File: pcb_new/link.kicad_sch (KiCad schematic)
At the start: 90 parts, among them J1 STLINK-V3MINIE, J11 68021-204HLF, J12 68021-204HLF, J13 68021-204HLF, J15 68021-204HLF, J16 68021-204HLF, J17 68021-204HLF, J18 68021-204HLF, SW1 TL6400AF160QJ, U1 STM32F479VGT6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

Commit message: initial test of new board
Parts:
- C32, C33, C34: Mouser Part Number 81-GRM15C61E475ME15J -> (none)
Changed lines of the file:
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@@
 			)
 		)
-		(property "Mouser Part Number" "81-GRM15C61E475ME15J"
+		(property "Mouser Part Number" ""
 			(at 388.62 806.68 0)
 			(effects
@@
 			)
 		)
-		(property "Mouser Part Number" "81-GRM15C61E475ME15J"
+		(property "Mouser Part Number" ""
 			(at 388.62 796.52 0)
 			(effects
@@
 			)
 		)
-		(property "Mouser Part Number" "81-GRM15C61E475ME15J"
+		(property "Mouser Part Number" ""
 			(at 388.62 801.6 0)
 			(effects

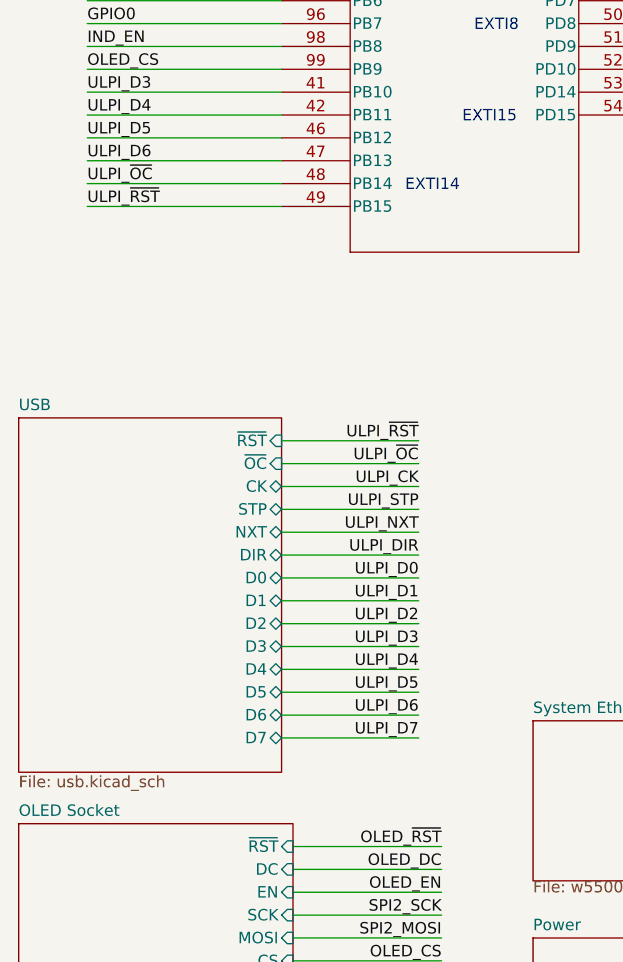
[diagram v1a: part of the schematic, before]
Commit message: don't mark `ULPI_~{OC}` as a ULPI netclass
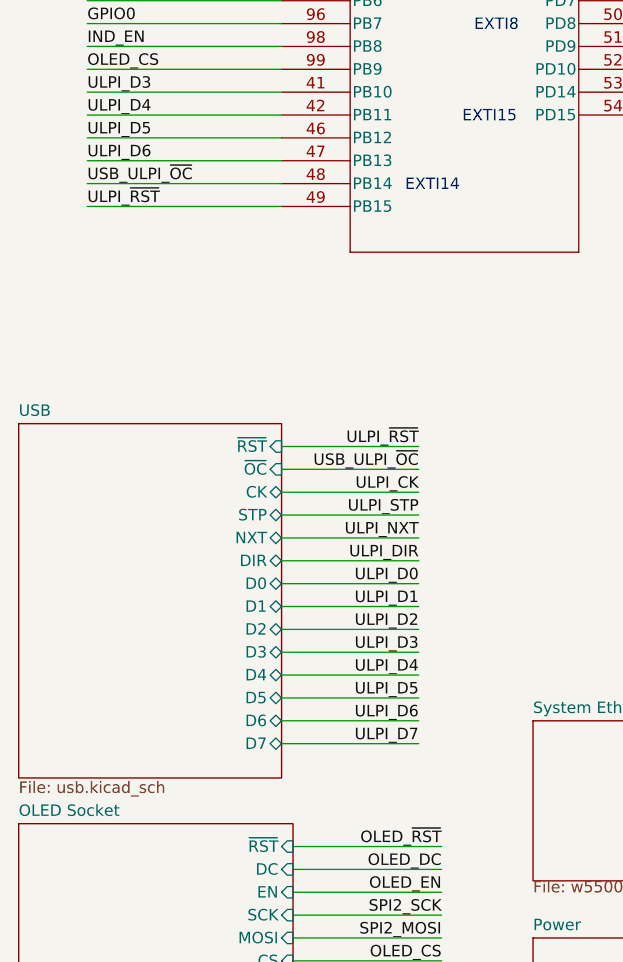
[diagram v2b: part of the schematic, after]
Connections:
- net ULPI_~{OC} renamed USB_ULPI_~{OC}
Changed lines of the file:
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@@
 	(wire
 		(pts
-			(xy 54.61 168.275) (xy 69.85 168.275)
+			(xy 54.61 168.91) (xy 69.85 168.91)
 		)
 		(stroke
@@
 	(wire
 		(pts
-			(xy 54.61 173.355) (xy 69.85 173.355)
+			(xy 54.61 173.99) (xy 69.85 173.99)
 		)
 		(stroke
@@
 	(wire
 		(pts
-			(xy 54.61 155.575) (xy 69.85 155.575)
+			(xy 54.61 156.21) (xy 69.85 156.21)
 		)
 		(stroke
@@
 	(wire
 		(pts
-			(xy 54.61 180.975) (xy 69.85 180.975)
+			(xy 54.61 181.61) (xy 69.85 181.61)
 		)
 		(stroke
@@
 	(wire
 		(pts
-			(xy 54.61 165.735) (xy 69.85 165.735)
+			(xy 54.61 166.37) (xy 69.85 166.37)
 		)
 		(stroke
@@
 	(wire
 		(pts
-			(xy 54.61 160.655) (xy 69.85 160.655)
+			(xy 54.61 161.29) (xy 69.85 161.29)
 		)
 		(stroke
@@
 	(wire
 		(pts
-			(xy 54.61 178.435) (xy 69.85 178.435)
+			(xy 54.61 179.07) (xy 69.85 179.07)
 		)
 		(stroke
@@
 	(wire
 		(pts
-			(xy 54.61 186.055) (xy 69.85 186.055)
+			(xy 54.61 186.69) (xy 69.85 186.69)
 		)
 		(stroke
@@
 	(wire
 		(pts
-			(xy 54.61 175.895) (xy 69.85 175.895)
+			(xy 54.61 176.53) (xy 69.85 176.53)
 		)
 		(stroke
@@
 	(wire
 		(pts
-			(xy 54.61 170.815) (xy 69.85 170.815)
+			(xy 54.61 171.45) (xy 69.85 171.45)
 		)
 		(stroke
@@
 	(wire
 		(pts
-			(xy 54.61 183.515) (xy 69.85 183.515)
+			(xy 54.61 184.15) (xy 69.85 184.15)
 		)
 		(stroke
@@
 	(wire
 		(pts
-			(xy 54.61 158.115) (xy 69.85 158.115)
+			(xy 54.61 158.75) (xy 69.85 158.75)
 		)
 		(stroke
@@
 	(wire
 		(pts
-			(xy 54.61 188.595) (xy 69.85 188.595)
+			(xy 54.61 189.23) (xy 69.85 189.23)
 		)
 		(stroke
@@
 	(wire
 		(pts
-			(xy 54.61 163.195) (xy 69.85 163.195)
+			(xy 54.61 163.83) (xy 69.85 163.83)
 		)
 		(stroke
@@
 	)
 	(label "ULPI_D2"
-		(at 69.85 175.895 180)
+		(at 69.85 176.53 180)
 		(fields_autoplaced yes)
 		(effects
@@
 	)
 	(label "ULPI_D1"
-		(at 69.85 173.355 180)
+		(at 69.85 173.99 180)
 		(fields_autoplaced yes)
 		(effects
@@
 		)
 	)
-	(label "OLED_CS"
-		(at 162.56 146.05 0)
+	(label "USB_ULPI_~{OC}"
+		(at 69.85 158.75 180)
 		(fields_autoplaced yes)
 		(effects
@@
 				(size 1.27 1.27)
 			)
-			(justify left bottom)
+			(justify right bottom)
 		)
 	)
-	(label "RS232_TX"
-		(at 187.96 273.05 0)
+	(label "OLED_CS"
+		(at 162.56 146.05 0)
 		(fields_autoplaced yes)
 		(effects
@@
 		)
 	)
-	(label "SPI3_MISO"
-		(at 74.93 233.68 180)
+	(label "RS232_TX"
+		(at 187.96 273.05 0)
 		(fields_autoplaced yes)
 		(effects
@@
 				(size 1.27 1.27)
 			)
-			(justify right bottom)
+			(justify left bottom)
 		)
 	)
-	(label "ULPI_~{OC}"
-		(at 69.85 158.115 180)
+	(label "SPI3_MISO"
+		(at 74.93 233.68 180)
 		(fields_autoplaced yes)
 		(effects
@@
 	)
 	(label "ULPI_D5"
-		(at 69.85 183.515 180)
+		(at 69.85 184.15 180)
 		(fields_autoplaced yes)
 		(effects
@@
 	)
 	(label "ULPI_CK"
-		(at 69.85 160.655 180)
+		(at 69.85 161.29 180)
 		(fields_autoplaced yes)
 		(effects
@@
 	)
 	(label "ULPI_NXT"
-		(at 69.85 165.735 180)
+		(at 69.85 166.37 180)
 		(fields_autoplaced yes)
 		(effects
@@
 		)
 	)
-	(label "ULPI_~{OC}"
+	(label "USB_ULPI_~{OC}"
 		(at 33.02 127 0)
 		(fields_autoplaced yes)
@@
 	)
 	(label "ULPI_D3"
-		(at 69.85 178.435 180)
+		(at 69.85 179.07 180)
 		(fields_autoplaced yes)
 		(effects
@@
 	)
 	(label "ULPI_D6"
-		(at 69.85 186.055 180)
+		(at 69.85 186.69 180)
 		(fields_autoplaced yes)
 		(effects
@@
 	)
 	(label "ULPI_DIR"
-		(at 69.85 168.275 180)
+		(at 69.85 168.91 180)
 		(fields_autoplaced yes)
 		(effects
@@
 	)
 	(label "ULPI_STP"
-		(at 69.85 163.195 180)
+		(at 69.85 163.83 180)
 		(fields_autoplaced yes)
 		(effects
@@
 	)
 	(label "ULPI_D0"
-		(at 69.85 170.815 180)
+		(at 69.85 171.45 180)
 		(fields_autoplaced yes)
 		(effects
@@
 	)
 	(label "ULPI_D4"
-		(at 69.85 180.975 180)
+		(at 69.85 181.61 180)
 		(fields_autoplaced yes)
 		(effects
@@
 	)
 	(label "ULPI_~{RST}"
-		(at 69.85 155.575 180)
+		(at 69.85 156.21 180)
 		(fields_autoplaced yes)
 		(effects
@@
 	)
 	(label "ULPI_D7"
-		(at 69.85 188.595 180)
+		(at 69.85 189.23 180)
 		(fields_autoplaced yes)
 		(effects
@@
 	)
 	(sheet
-		(at 25.4 153.035)
+		(at 25.4 153.67)
 		(size 29.21 39.37)
 		(fields_autoplaced yes)
@@
 		)
 		(property "Sheetname" "USB"
-			(at 25.4 152.3234 0)
+			(at 25.4 152.9584 0)
 			(effects
 				(font
@@
 		)
 		(property "Sheetfile" "usb.kicad_sch"
-			(at 25.4 192.7356 0)
+			(at 25.4 193.3706 0)
 			(effects
 				(font
@@
 		)
 		(pin "CK" bidirectional
-			(at 54.61 160.655 0)
+			(at 54.61 161.29 0)
 			(effects
 				(font
@@
 		)
 		(pin "STP" bidirectional
-			(at 54.61 163.195 0)
+			(at 54.61 163.83 0)
 			(effects
 				(font
@@
 		)
 		(pin "NXT" bidirectional
-			(at 54.61 165.735 0)
+			(at 54.61 166.37 0)
 			(effects
 				(font
@@
 		)
 		(pin "DIR" bidirectional
-			(at 54.61 168.275 0)
+			(at 54.61 168.91 0)
 			(effects
 				(font
@@
 		)
 		(pin "D5" bidirectional
-			(at 54.61 183.515 0)
+			(at 54.61 184.15 0)
 			(effects
 				(font
@@
 		)
 		(pin "D4" bidirectional
-			(at 54.61 180.975 0)
+			(at 54.61 181.61 0)
 			(effects
 				(font
@@
 		)
 		(pin "D6" bidirectional
-			(at 54.61 186.055 0)
+			(at 54.61 186.69 0)
 			(effects
 				(font
@@
 		)
 		(pin "D0" bidirectional
-			(at 54.61 170.815 0)
+			(at 54.61 171.45 0)
 			(effects
 				(font
@@
 		)
 		(pin "D3" bidirectional
-			(at 54.61 178.435 0)
+			(at 54.61 179.07 0)
 			(effects
 				(font
@@
 		)
 		(pin "D2" bidirectional
-			(at 54.61 175.895 0)
+			(at 54.61 176.53 0)
 			(effects
 				(font
@@
 		)
 		(pin "D1" bidirectional
-			(at 54.61 173.355 0)
+			(at 54.61 173.99 0)
 			(effects
 				(font
@@
 		)
 		(pin "~{OC}" input
-			(at 54.61 158.115 0)
+			(at 54.61 158.75 0)
 			(effects
 				(font
@@
 		)
 		(pin "D7" bidirectional
-			(at 54.61 188.595 0)
+			(at 54.61 189.23 0)
 			(effects
 				(font
@@
 		)
 		(pin "~{RST}" input
-			(at 54.61 155.575 0)
+			(at 54.61 156.21 0)
 			(effects
 				(font

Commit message: add power monitor alert interrupt line (ref #82)
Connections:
- net GPIO4: no longer names the net of J15.1
- net GPIO4: no longer U1.34 (PE9)
- new net ~{POWER_ALERT}: U1.34 (PE9)
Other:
- sheet Power ports: added ~{ALERT}; removed none
- note added: "EXTI9"
- note added: "TBD"
- moved on the sheet: R1, R2

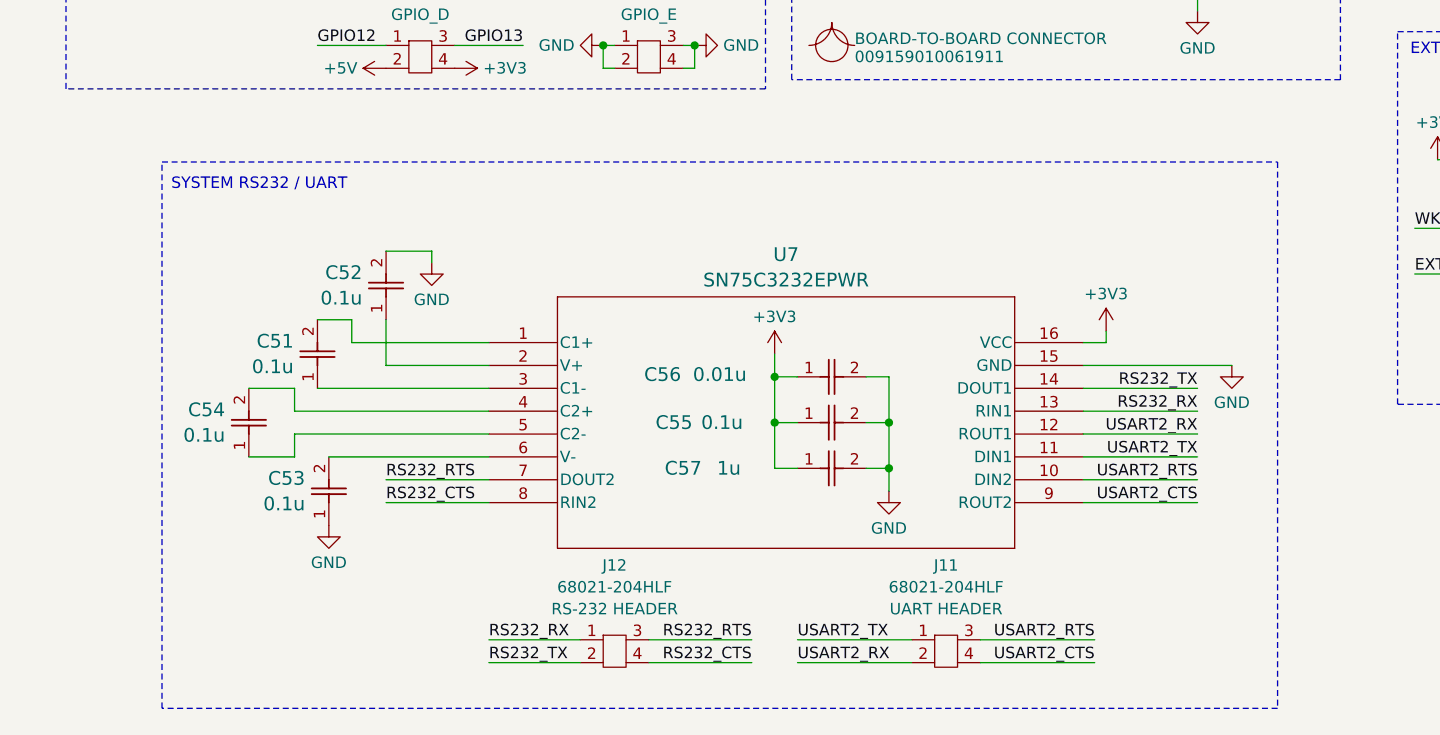
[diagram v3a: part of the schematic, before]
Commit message: add pullup on USART CTS/TX lines (ref #67)
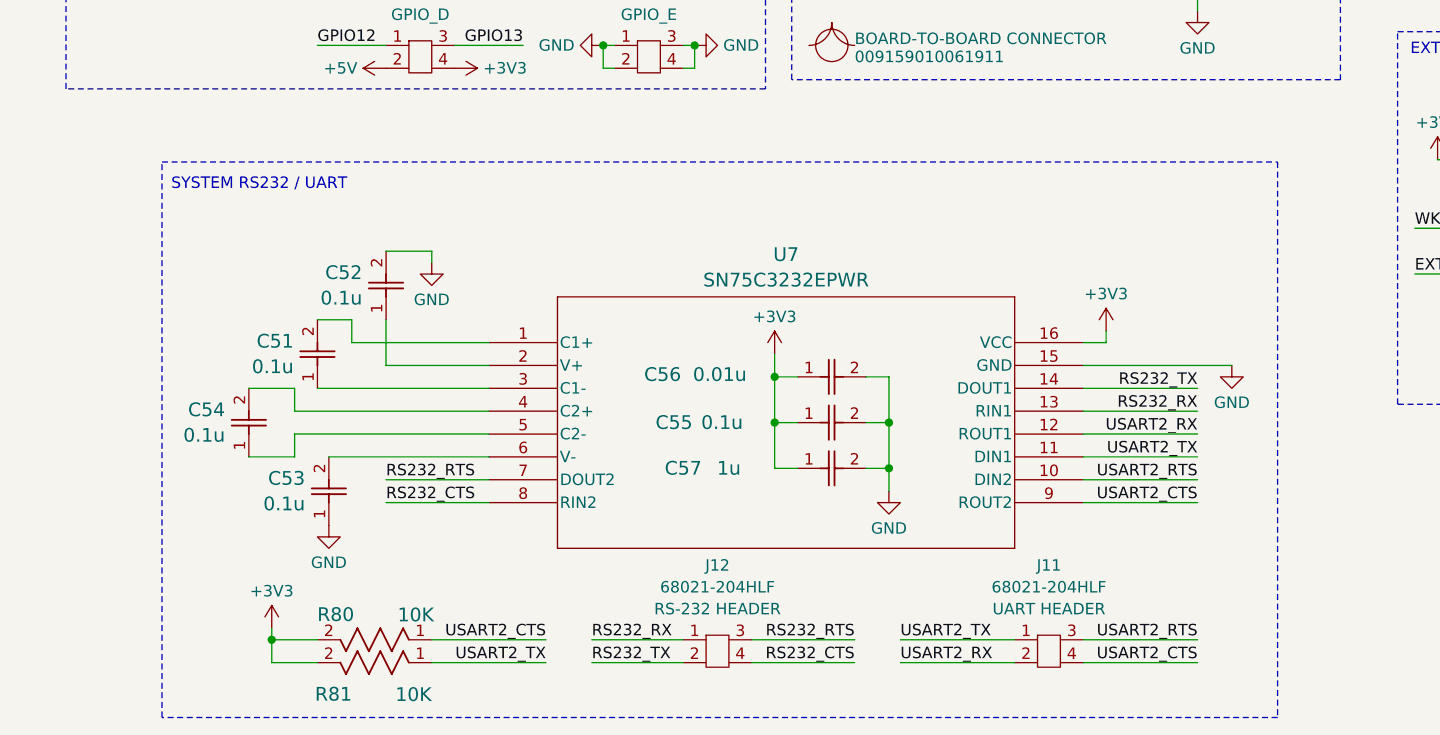
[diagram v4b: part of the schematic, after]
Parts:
- added R80, R81: 10K, OroLink:STA_RMCF0402_STP, symbol OroLink:RMCF0402FT10K0
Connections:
- net +3V3: now also R80.2, R81.2
- net USART2_CTS: now also R80.1
- net USART2_TX: now also R81.1
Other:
- moved on the sheet: J11, J12

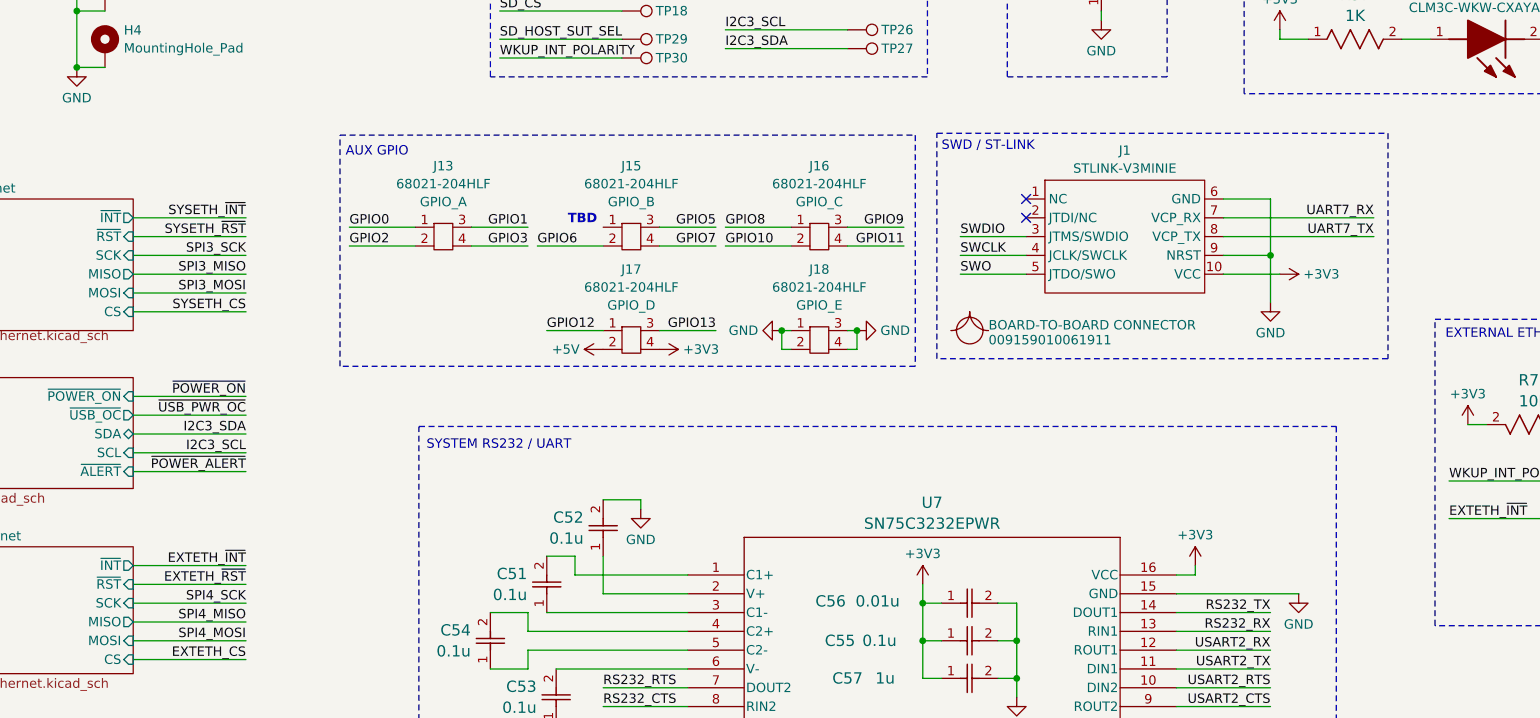
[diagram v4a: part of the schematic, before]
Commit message: pull up external ethernet ~{RST} line (ref #74)
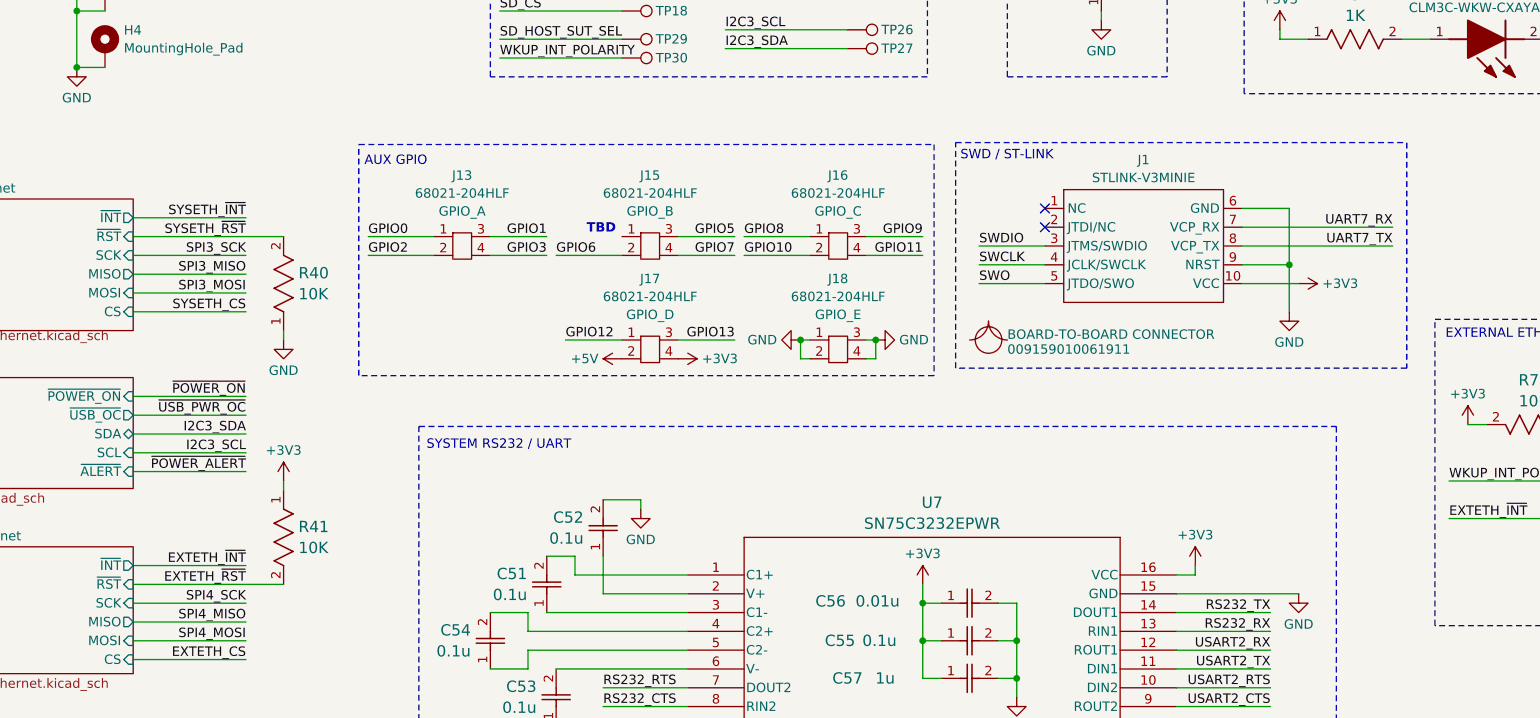
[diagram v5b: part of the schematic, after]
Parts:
- added R40, R41: 10K, OroLink:STA_RMCF0402_STP, symbol OroLink:RMCF0402FT10K0
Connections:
- net +3V3: now also R41.1
- net EXTETH_~{RST}: now also R41.2
- net GND: now also R40.1
- net SYSETH_~{RST}: now also R40.2
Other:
- moved on the sheet: J1, J13, J15, J16, J17, J18
